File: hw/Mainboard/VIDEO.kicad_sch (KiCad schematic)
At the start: 1 part, among them J9 VIDEO

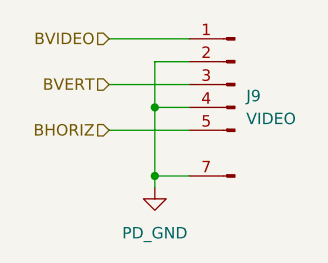
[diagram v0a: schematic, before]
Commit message: hw: 9V DC plug on left edge, change default track size
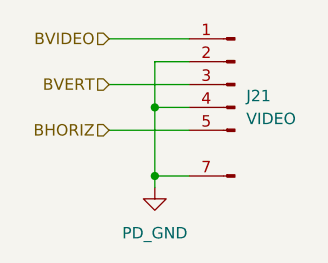
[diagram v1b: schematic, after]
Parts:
- renumbered J9 to J21
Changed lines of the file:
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@@
   (symbol (lib_id "PET:PD_GND") (at 137.16 101.6 0) (unit 1)
     (in_bom yes) (on_board yes) (fields_autoplaced)
-    (property "Reference" "#PWR0163" (id 0) (at 137.16 107.95 0)
+    (property "Reference" "#PWR0123" (id 0) (at 137.16 107.95 0)
       (effects (font (size 1.27 1.27)) hide)
     )
@@
   (symbol (lib_id "Retrocomputing:CBM_PET_VIDEO_Conn_Keyed") (at 146.05 92.71 0) (mirror y) (unit 1)
     (in_bom yes) (on_board yes) (fields_autoplaced)
-    (property "Reference" "J9" (id 0) (at 147.32 91.4399 0)
+    (property "Reference" "J21" (id 0) (at 147.32 91.4399 0)
       (effects (font (size 1.27 1.27)) (justify right))
     )

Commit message: hw: 25x2 header (wip)
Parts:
- renumbered J21 to J22
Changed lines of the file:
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@@
   (symbol (lib_id "PET:PD_GND") (at 137.16 101.6 0) (unit 1)
     (in_bom yes) (on_board yes) (fields_autoplaced)
-    (property "Reference" "#PWR0123" (id 0) (at 137.16 107.95 0)
+    (property "Reference" "#PWR0125" (id 0) (at 137.16 107.95 0)
       (effects (font (size 1.27 1.27)) hide)
     )
@@
   (symbol (lib_id "Retrocomputing:CBM_PET_VIDEO_Conn_Keyed") (at 146.05 92.71 0) (mirror y) (unit 1)
     (in_bom yes) (on_board yes) (fields_autoplaced)
-    (property "Reference" "J21" (id 0) (at 147.32 91.4399 0)
+    (property "Reference" "J22" (id 0) (at 147.32 91.4399 0)
       (effects (font (size 1.27 1.27)) (justify right))
     )

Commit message: hw: 2x config switch (wip)
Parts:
- renumbered J22 to J21
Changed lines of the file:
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@@
   (symbol (lib_id "PET:PD_GND") (at 137.16 101.6 0) (unit 1)
     (in_bom yes) (on_board yes) (fields_autoplaced)
-    (property "Reference" "#PWR0125" (id 0) (at 137.16 107.95 0)
+    (property "Reference" "#PWR0131" (id 0) (at 137.16 107.95 0)
       (effects (font (size 1.27 1.27)) hide)
     )
@@
   (symbol (lib_id "Retrocomputing:CBM_PET_VIDEO_Conn_Keyed") (at 146.05 92.71 0) (mirror y) (unit 1)
     (in_bom yes) (on_board yes) (fields_autoplaced)
-    (property "Reference" "J22" (id 0) (at 147.32 91.4399 0)
+    (property "Reference" "J21" (id 0) (at 147.32 91.4399 0)
       (effects (font (size 1.27 1.27)) (justify right))
     )

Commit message: hw: caps & logos (wip)
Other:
- title: CBM PET Mainboard Replacement -> EconoPET 40/8096
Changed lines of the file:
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@@
   (paper "A")
   (title_block
-    (title "CBM PET Mainboard Replacement")
+    (title "EconoPET 40/8096")
+    (date "2023-10-01")
+    (rev "A")
   )
   (junction (at 137.16 92.71) (diameter 0) (color 0 0 0 0)

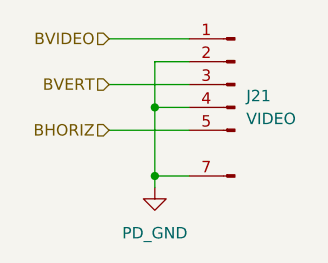
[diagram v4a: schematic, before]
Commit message: hw: renumber J* refs to match PET connectors
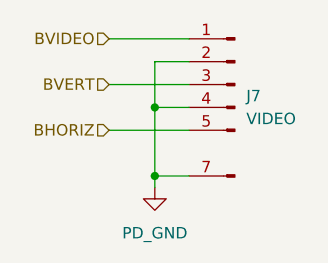
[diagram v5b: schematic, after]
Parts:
- renumbered J21 to J7
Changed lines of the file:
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@@
   (symbol (lib_id "PET:PD_GND") (at 137.16 101.6 0) (unit 1)
     (in_bom yes) (on_board yes) (fields_autoplaced)
-    (property "Reference" "#PWR0131" (id 0) (at 137.16 107.95 0)
+    (property "Reference" "#PWR0143" (id 0) (at 137.16 107.95 0)
       (effects (font (size 1.27 1.27)) hide)
     )
@@
   (symbol (lib_id "Retrocomputing:CBM_PET_VIDEO_Conn_Keyed") (at 146.05 92.71 0) (mirror y) (unit 1)
     (in_bom yes) (on_board yes) (fields_autoplaced)
-    (property "Reference" "J21" (id 0) (at 147.32 91.4399 0)
+    (property "Reference" "J7" (id 0) (at 147.32 91.4399 0)
       (effects (font (size 1.27 1.27)) (justify right))
     )
